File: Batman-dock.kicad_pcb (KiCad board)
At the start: 2 copper layers, 42 x 12 mm, 5 parts, among them J1 TYPEC-324-BCP24, J2 70AAJ-6-M0G, J3 70AAJ-6-M0G

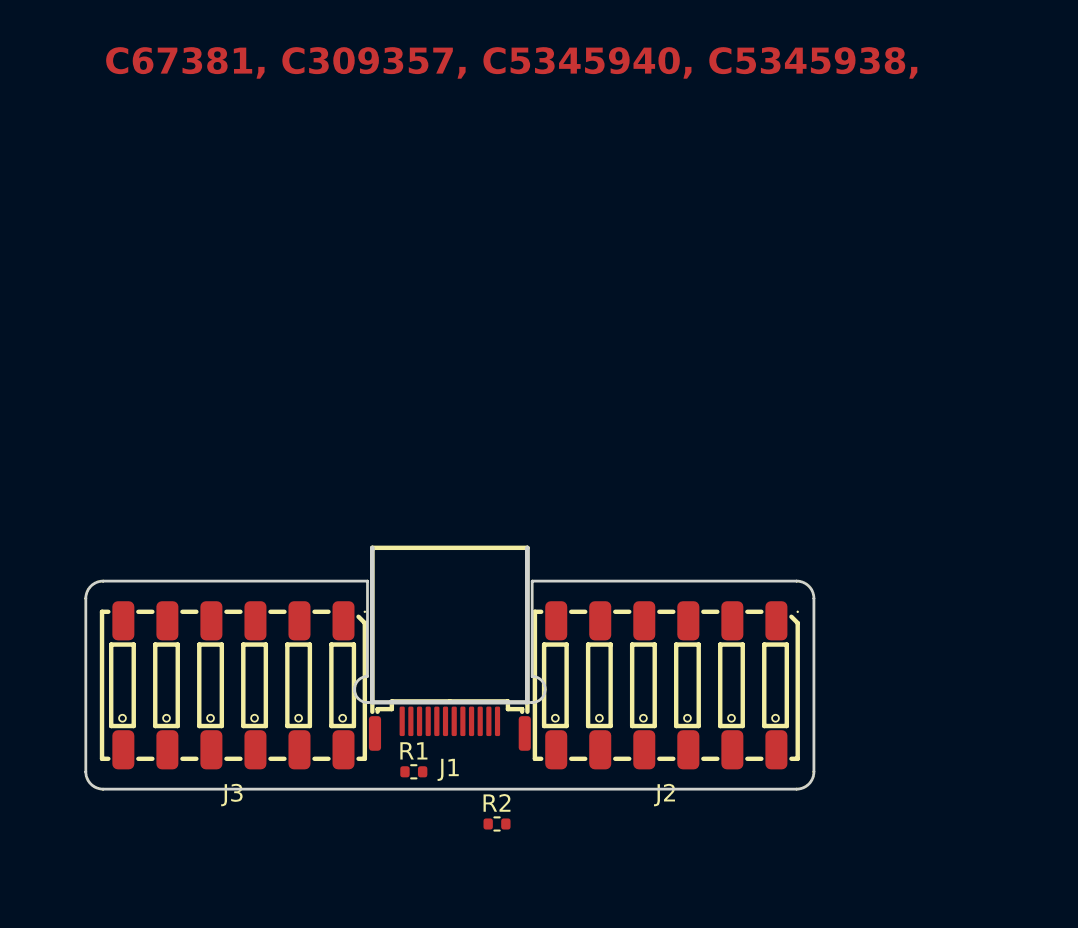
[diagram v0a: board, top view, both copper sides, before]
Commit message: Kicad 9. Added usb and spring footprint.
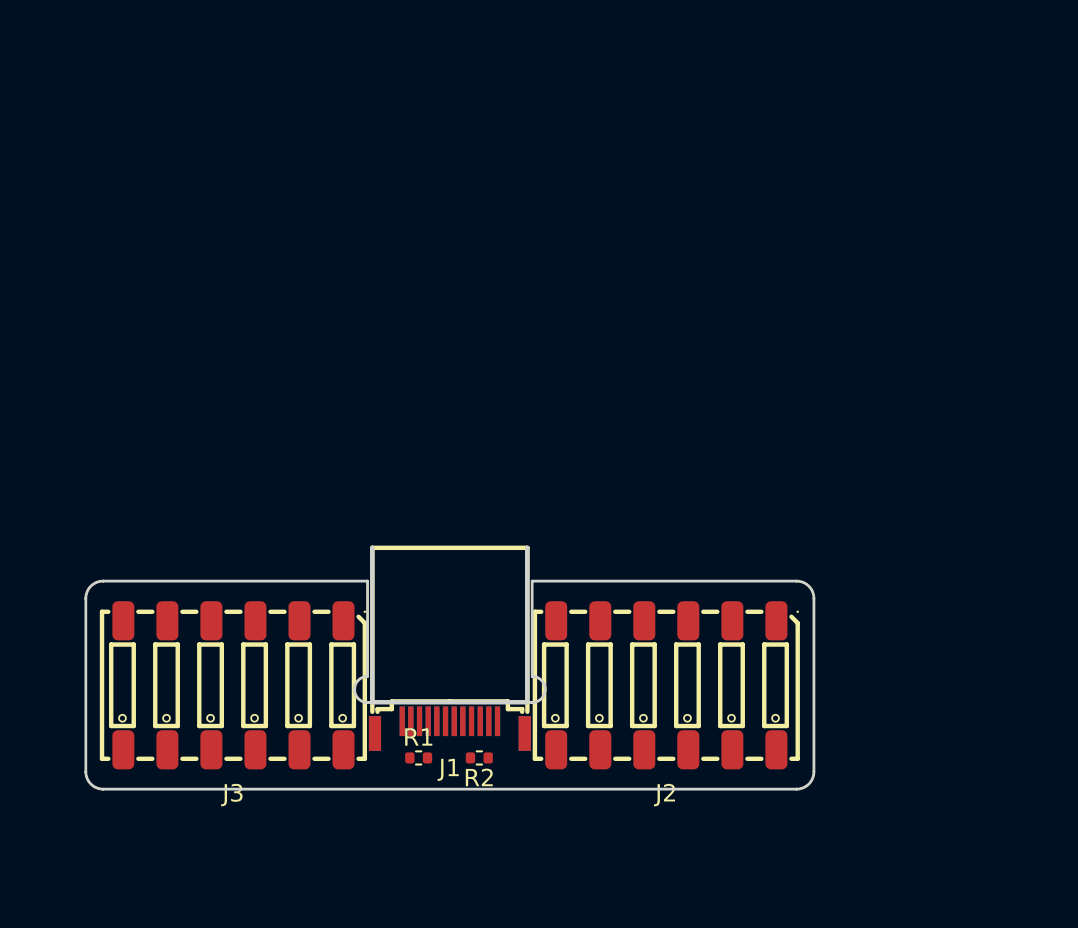
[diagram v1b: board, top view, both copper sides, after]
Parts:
- J1: footprint USB-TYPE-C-SMD_USB-307HG-B-SU -> jlc:USB-TYPE-C-SMD_USB-307HG-B-SU
- moved R2 3.94 mm to (123.9, 98.5), turned to 180 degrees
- moved R1 0.85 mm to (120.4, 98.5)

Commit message: Shield
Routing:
- net Net-(J1-CC1): track 0.00 -> 2.66 mm, vias 0 -> 1
- net Net-(J1-CC2): track 0.00 -> 2.29 mm
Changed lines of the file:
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@@
 			(pintype "passive")
 		)
-		(pad "SH" smd rect
+		(pad "S1" smd rect
 			(at -4.319914 -0.350013)
 			(size 0.7 2)
 			(layers "F.Cu" "F.Mask" "F.Paste")
-		)
-		(pad "SH" smd rect
+			(net 26 "GND")
+			(pinfunction "SHIELD")
+			(pintype "passive")
+		)
+		(pad "S1" smd rect
 			(at -4.319914 -0.350013)
 			(size 0.7 2)
 			(layers "B.Cu" "B.Mask" "B.Paste")
-		)
-		(pad "SH" smd rect
+			(net 26 "GND")
+			(pinfunction "SHIELD")
+			(pintype "passive")
+		)
+		(pad "S1" smd rect
 			(at 4.319914 -0.350013)
 			(size 0.7 2)
 			(layers "F.Cu" "F.Mask" "F.Paste")
-		)
-		(pad "SH" smd rect
+			(net 26 "GND")
+			(pinfunction "SHIELD")
+			(pintype "passive")
+		)
+		(pad "S1" smd rect
 			(at 4.319914 -0.350013)
 			(size 0.7 2)
 			(layers "B.Cu" "B.Mask" "B.Paste")
+			(net 26 "GND")
+			(pinfunction "SHIELD")
+			(pintype "passive")
 		)
 		(embedded_fonts no)
 		(model "packages3d/USB-TYPE-C-SMD_USB-307HG-B-SU.step"
 			(offset
-				(xyz 0 -1 -0.5)
+				(xyz -0.0000253999996185 0.7501381887 -0.399999194)
 			)
 			(scale
@@
 			)
 			(rotate
-				(xyz -90 -0 -0)
+				(xyz -90 0 0)
 			)
 		)
@@
 		)
 	)
+	(segment
+		(start 123.42 98.52)
+		(end 122.979936 98.079936)
+		(width 0.3)
+		(layer "F.Cu")
+		(net 31)
+	)
+	(segment
+		(start 122.979936 98.079936)
+		(end 122.979936 96.408059)
+		(width 0.3)
+		(layer "F.Cu")
+		(net 31)
+	)
+	(segment
+		(start 121.04 98.42)
+		(end 120.94 98.52)
+		(width 0.3)
+		(layer "F.Cu")
+		(net 35)
+	)
+	(segment
+		(start 121.53 98.42)
+		(end 121.04 98.42)
+		(width 0.3)
+		(layer "F.Cu")
+		(net 35)
+	)
+	(via
+		(at 121.53 98.42)
+		(size 0.6)
+		(drill 0.3)
+		(layers "F.Cu" "B.Cu")
+		(net 35)
+	)
+	(segment
+		(start 121.53 98.42)
+		(end 121.478793 98.368793)
+		(width 0.3)
+		(layer "B.Cu")
+		(net 35)
+	)
+	(segment
+		(start 121.478793 98.368793)
+		(end 121.478793 96.408059)
+		(width 0.3)
+		(layer "B.Cu")
+		(net 35)
+	)
 	(embedded_fonts no)

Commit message: Batman routing
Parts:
- J1: value TYPEC-324-BCP24 -> TYPECL324LBCP24
- J2, J3: value 70AAJ-6-M0G -> 70AAJL6LM0G
- moved R2 1.19 mm to (122.9, 99.2), turned to 45 degrees
- moved R1 1.15 mm to (121.4, 99.2), turned to 135 degrees
- moved J3 0.19 mm to (109.9, 94.3)
- moved J2 0.18 mm to (134.5, 94.3)
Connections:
- J1 pad A4: +12V -> VBUS
- J1 pad A9: +12V -> VBUS
- J1 pad B4: +12V -> VBUS
- J1 pad B9: +12V -> VBUS
- J2 pad 1: unconnected-(J2-Pad1) -> VBUS
- J2 pad 10: unconnected-(J2-Pad10) -> CAN2_H
- J2 pad 11: unconnected-(J2-Pad11) -> SBU2
- J2 pad 12: unconnected-(J2-Pad12) -> VBUS
- J2 pad 2: unconnected-(J2-Pad2) -> SBU2
- J2 pad 3: unconnected-(J2-Pad3) -> CAN2_H
- J2 pad 4: unconnected-(J2-Pad4) -> CAN2_L
- J2 pad 5: unconnected-(J2-Pad5) -> CAN1_H
- J2 pad 6: unconnected-(J2-Pad6) -> CAN1_L
- J2 pad 7: unconnected-(J2-Pad7) -> CAN1_L
- J2 pad 8: unconnected-(J2-Pad8) -> CAN1_H
- J2 pad 9: unconnected-(J2-Pad9) -> CAN2_L
- J3 pad 1: unconnected-(J3-Pad1) -> CAN3_L
- J3 pad 10: unconnected-(J3-Pad10) -> CAN0_L
- J3 pad 11: unconnected-(J3-Pad11) -> CAN3_H
- J3 pad 12: unconnected-(J3-Pad12) -> CAN3_L
- J3 pad 2: unconnected-(J3-Pad2) -> CAN3_H
- J3 pad 3: unconnected-(J3-Pad3) -> CAN0_L
- J3 pad 4: unconnected-(J3-Pad4) -> CAN0_H
- J3 pad 5: unconnected-(J3-Pad5) -> SBU1
- J3 pad 6: unconnected-(J3-Pad6) -> GND
- J3 pad 7: unconnected-(J3-Pad7) -> GND
- J3 pad 8: unconnected-(J3-Pad8) -> SBU1
- J3 pad 9: unconnected-(J3-Pad9) -> CAN0_H
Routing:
- net GND: track 0.00 -> 47.1 mm, vias 0 -> 29
- net VBUS: track 0.00 -> 44.5 mm, vias 0 -> 7
- net SBU2: track 0.00 -> 28.3 mm, vias 0 -> 2
- net SBU1: track 0.00 -> 27.1 mm, vias 0 -> 1
- net CAN0_H: track 0.00 -> 21.9 mm, vias 0 -> 1
- net CAN2_H: track 0.00 -> 21.4 mm, vias 0 -> 2
- net CAN2_L: track 0.00 -> 20.5 mm
- net CAN0_L: track 0.00 -> 19.4 mm, vias 0 -> 1
- net CAN1_H: track 0.00 -> 17.1 mm, vias 0 -> 1
- net CAN3_H: track 0.00 -> 15.3 mm, vias 0 -> 2
- net CAN1_L: track 0.00 -> 14.9 mm, vias 0 -> 1
- net CAN3_L: track 0.00 -> 13.6 mm
- added copper zone on B.Cu, net GND
- added copper zone on F.Cu, net GND
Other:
- outline, holes or cut-outs redrawn
- board text added: "Batman-dock Rev. ${REVISION}"

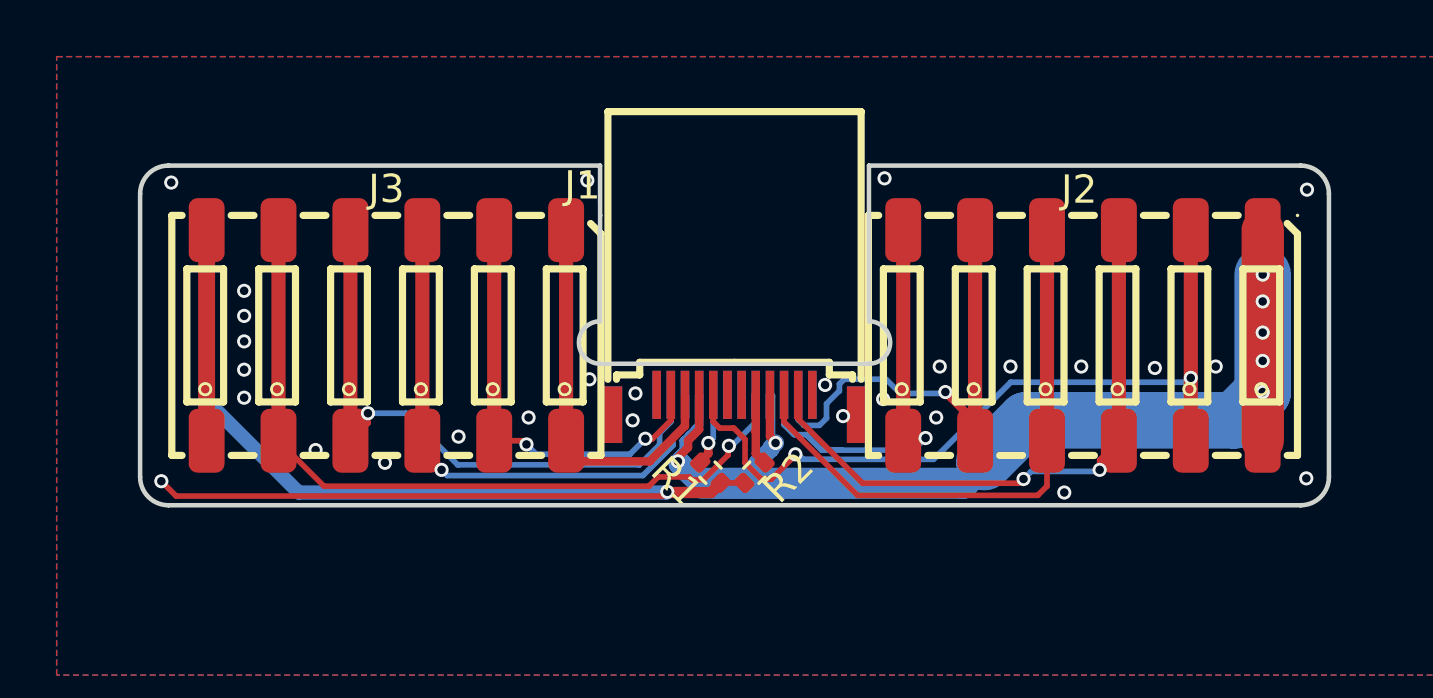
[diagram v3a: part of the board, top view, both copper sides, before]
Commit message: batman more clearance
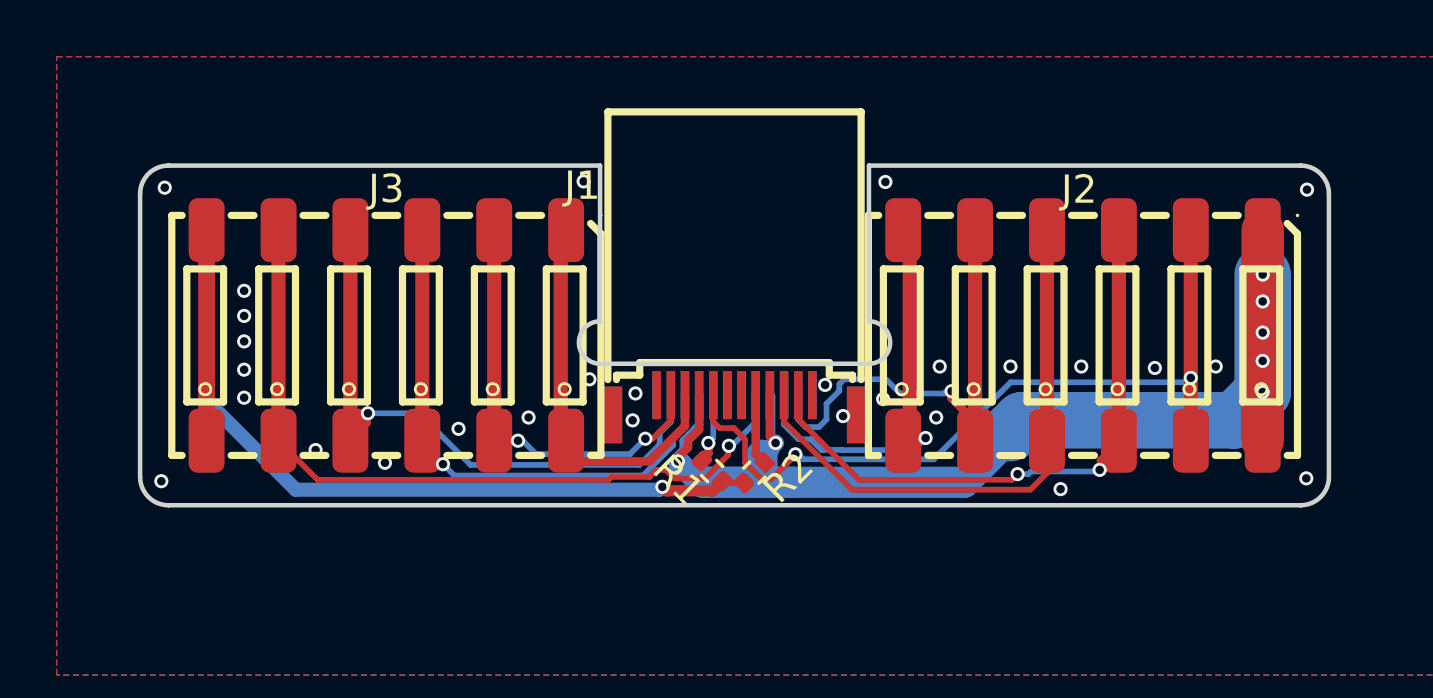
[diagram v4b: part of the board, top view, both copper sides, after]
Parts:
- moved R1 0.08 mm to (121.4, 99.1)
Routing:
- net GND: track 47.1 -> 29.0 mm
- net VBUS: track 44.5 -> 47.7 mm

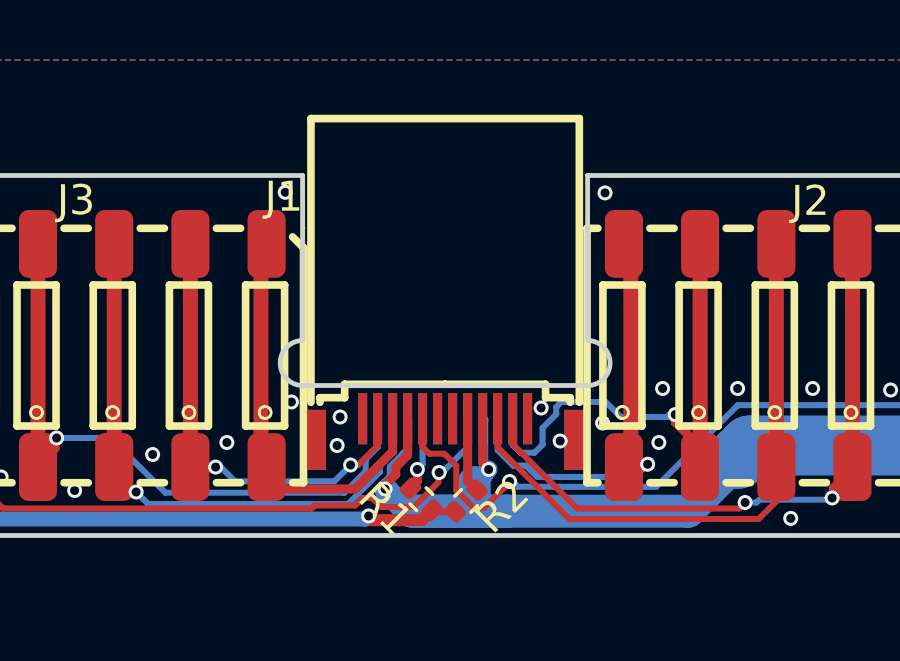
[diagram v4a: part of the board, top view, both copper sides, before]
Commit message: 1mm batman PCB
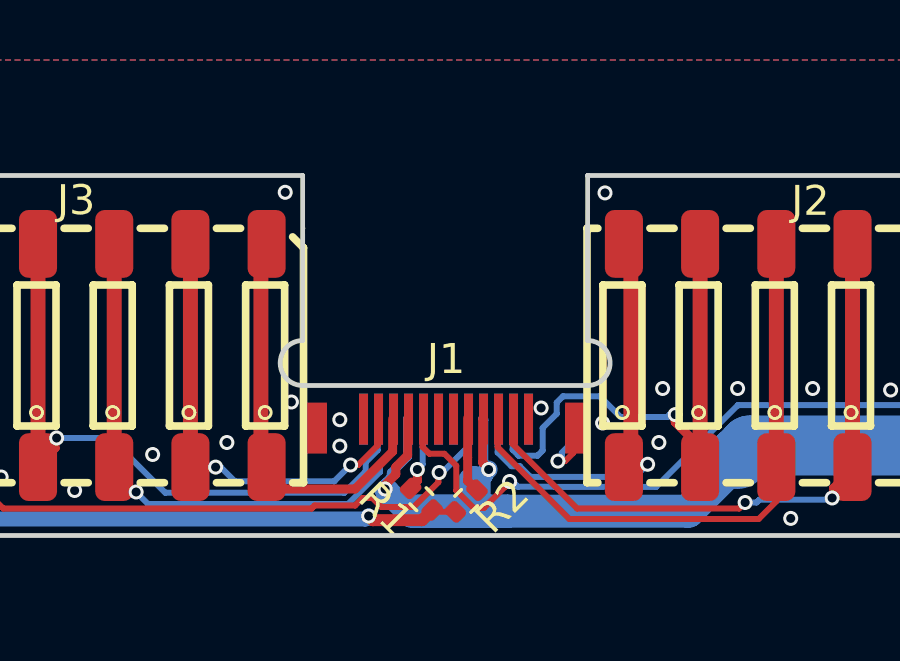
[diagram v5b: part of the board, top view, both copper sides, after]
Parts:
- J1: footprint jlc:USB-TYPE-C-SMD_USB-307HG-B-SU -> jlc:USB-SMD_HC-TYPE-C-24P-CP1.0-5A-L10.45-01
- moved J1 0.19 mm to (122.3, 96.6), turned to 0 degrees
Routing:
- net GND: track 29.0 -> 30.0 mm
- net CAN1_H: track 17.3 -> 17.9 mm
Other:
- board text added: "1mm: C67381, C309357, C5345940, C5345938, 0.8mm: C309352"
- board text removed: "C67381, C309357, C5345940, C5345938,"

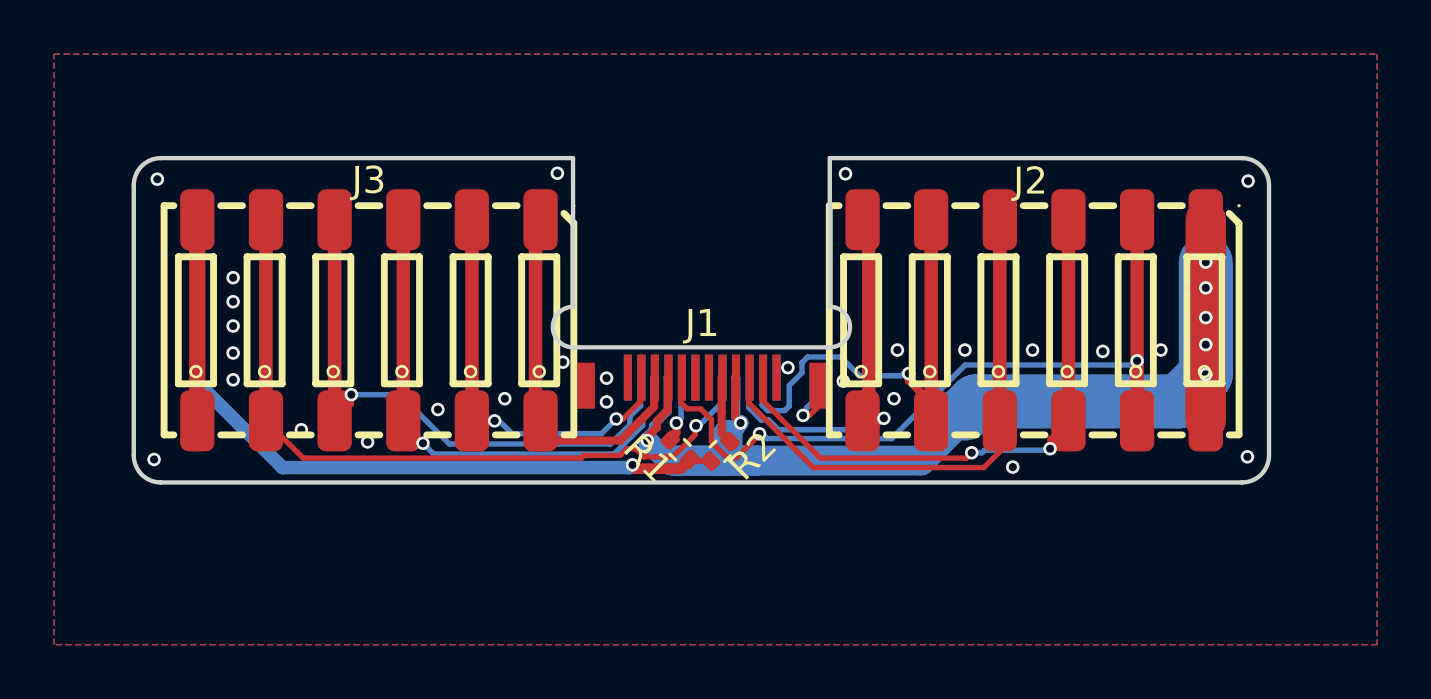
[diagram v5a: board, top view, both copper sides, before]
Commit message: Fixed CAN order RX<->TX flip. Less copper.
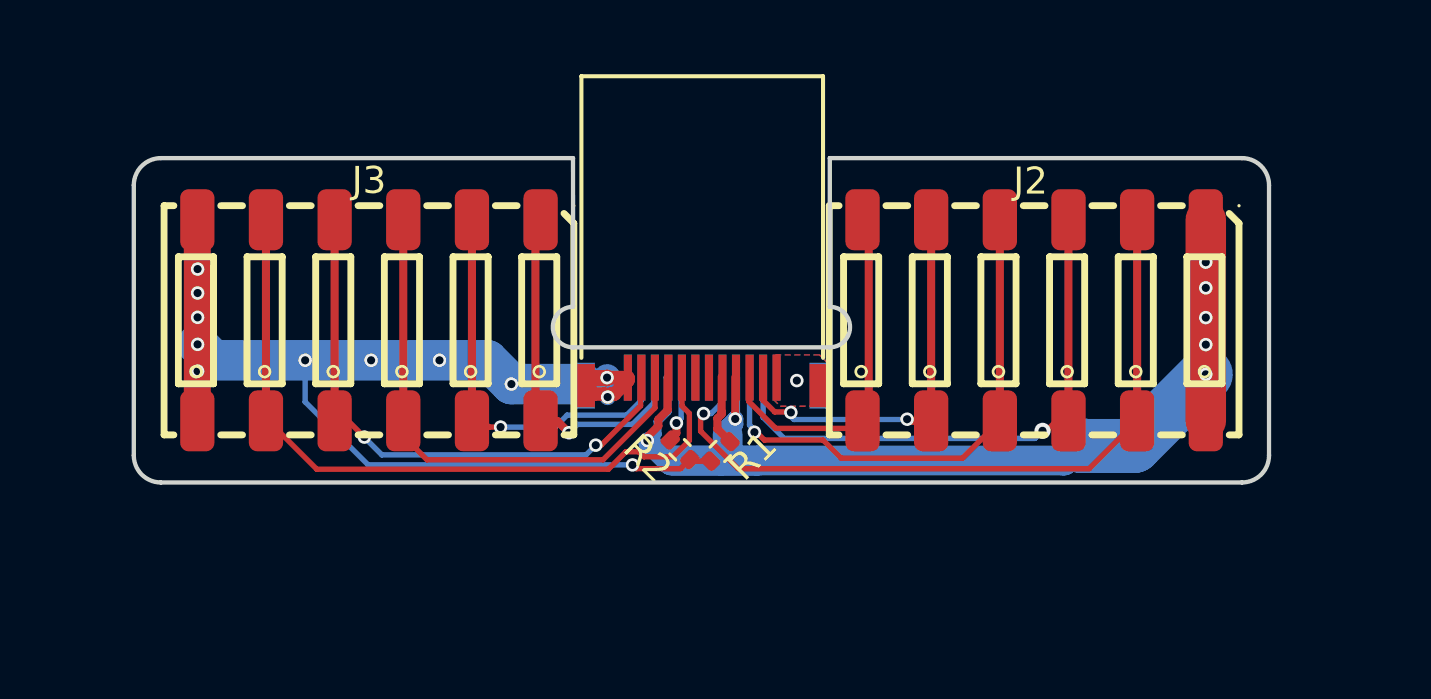
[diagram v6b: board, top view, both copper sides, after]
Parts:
- J1: moved to B.Cu
- turned J1 to 180 degrees
- renumbered R2 to R1, R1 to R2
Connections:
- J1 pad A10: CAN1_L -> CAN0_L
- J1 pad A11: CAN1_H -> CAN0_H
- J1 pad A2: CAN0_H -> CAN1_H
- J1 pad A3: CAN0_L -> CAN1_L
- J1 pad B10: CAN3_L -> CAN2_L
- J1 pad B11: CAN3_H -> CAN2_H
- J1 pad B2: CAN2_H -> CAN3_H
- J1 pad B3: CAN2_L -> CAN3_L
- R1 pad 2: Net-(J1-CC2) -> Net-(J1-CC1)
- R2 pad 2: Net-(J1-CC1) -> Net-(J1-CC2)
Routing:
- net GND: track 30.0 -> 50.2 mm, vias 29 -> 13
- net CAN1_H: track 17.9 -> 14.9 mm, vias 1 -> 2
- net CAN1_L: track 15.1 -> 12.9 mm, vias 1 -> 0
- net CAN0_H: track 21.9 -> 20.2 mm, vias 1 -> 2
- net SBU2: track 28.3 -> 27.4 mm, vias 2 -> 1
- net CAN2_L: track 20.1 -> 19.6 mm, vias 0 -> 1
- net CAN3_L: track 13.8 -> 13.4 mm, vias 0 -> 1
- net CAN2_H: track 21.3 -> 21.0 mm, vias 2 -> 1
- net CAN3_H: track 15.3 -> 15.1 mm, vias 2 -> 1
- net SBU1: track 27.1 -> 26.9 mm, vias 1 -> 0
- net CAN0_L: track 19.4 -> 19.6 mm, vias 1 -> 0
- net Net-(J1-CC1): track 2.51 -> 2.66 mm, vias 1 -> 0
- net Net-(J1-CC2): track 2.53 -> 2.51 mm, vias 0 -> 1
